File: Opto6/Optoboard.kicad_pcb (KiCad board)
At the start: 2 copper layers, 91.4 x 33 mm, 54 parts, among them J1 S1 Connector, J2 S2 Connector, J3 S3 Connector, J4 S4 Connector, J6 S5 Connector, J7 S6 Connector, P1 CONN_01X08, Q1 IRLR024NPBF, U1 6N135, U2 6N135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

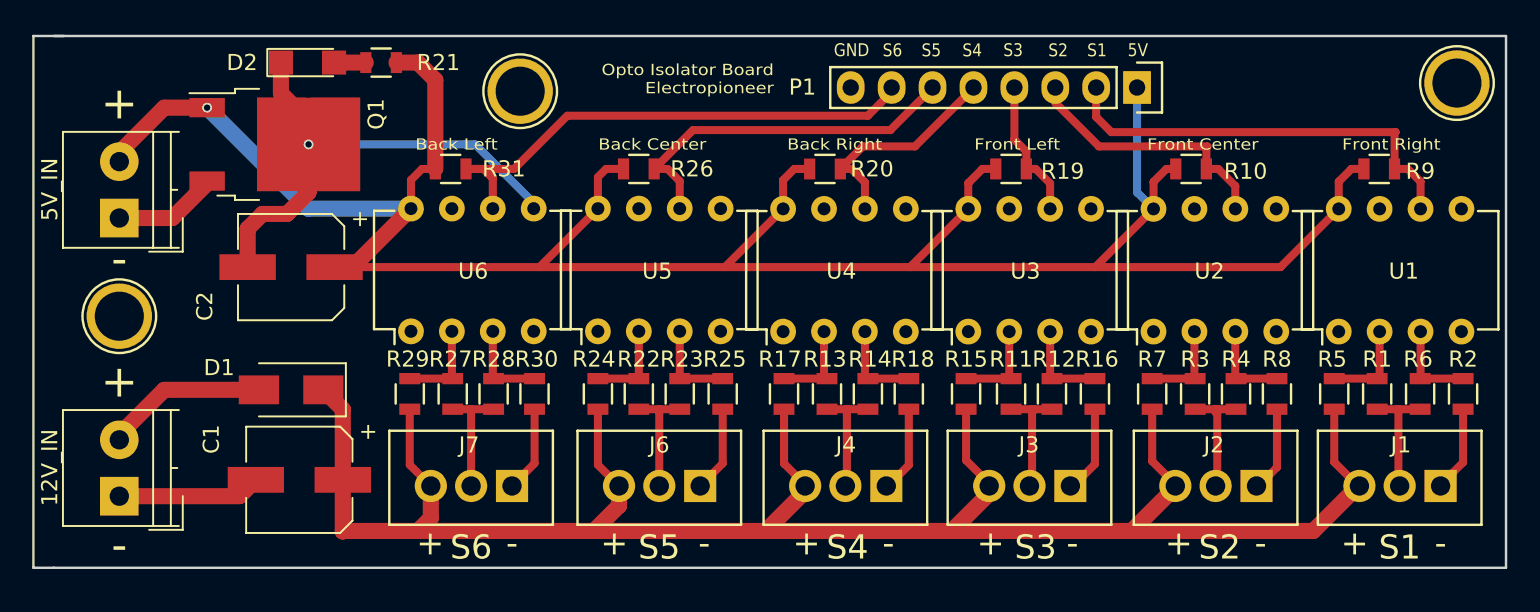
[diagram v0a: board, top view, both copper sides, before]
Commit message: Added opto4 and opto6 updated images
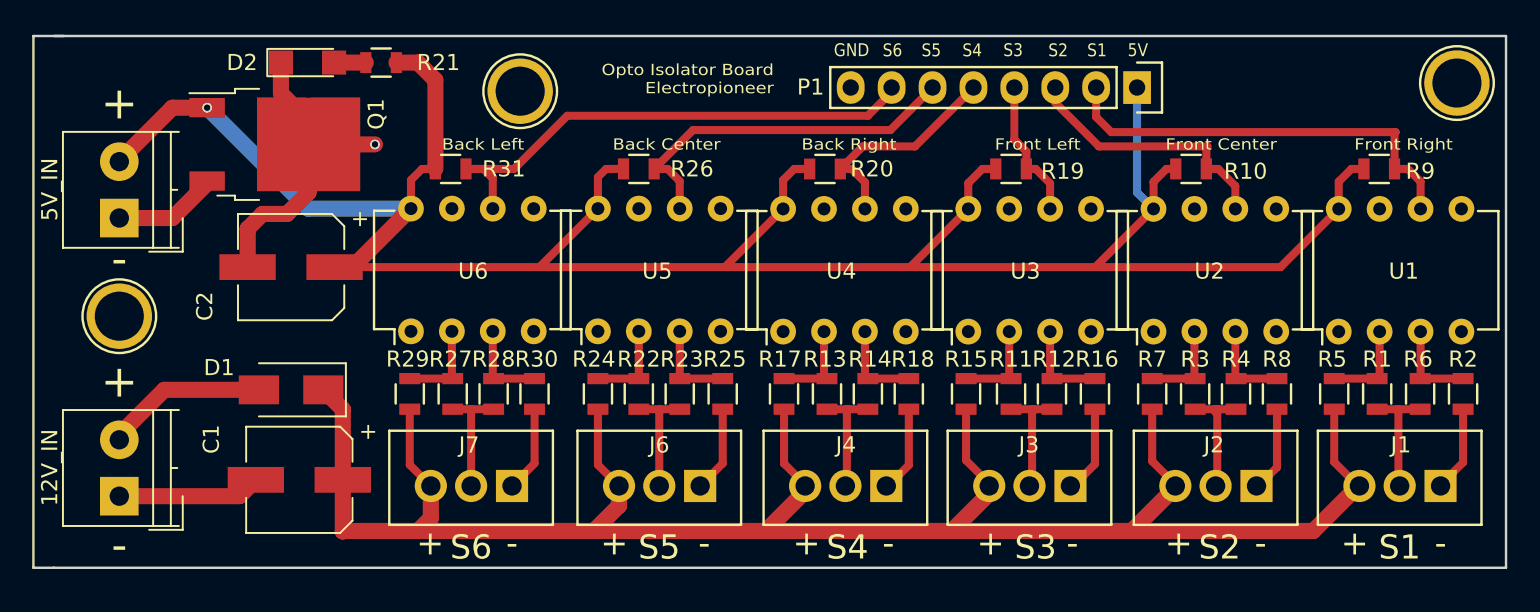
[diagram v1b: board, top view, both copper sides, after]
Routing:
- net GND: track 72.6 -> 61.2 mm
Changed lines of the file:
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@@
     (links 107)
     (no_connects 0)
-    (area 136.373799 90.069599 227.963801 123.239601)
+    (area 136.3398 88.236666 228.2968 125.673172)
     (thickness 1.6)
-    (drawings 46)
-    (tracks 221)
+    (drawings 49)
+    (tracks 220)
     (zones 0)
     (modules 54)
@@
     (32 B.Adhes user)
     (33 F.Adhes user)
-    (34 B.Paste user hide)
+    (34 B.Paste user)
     (35 F.Paste user)
     (36 B.SilkS user)
@@
     (38 B.Mask user)
     (39 F.Mask user)
-    (40 Dwgs.User user hide)
+    (40 Dwgs.User user)
     (41 Cmts.User user)
     (42 Eco1.User user)
@@
   )
   (setup
-    (last_trace_width 1)
+    (last_trace_width 0.25)
     (user_trace_width 0.25)
     (user_trace_width 0.5)
@@
     (pad_to_mask_clearance 0.2)
     (aux_axis_origin 0 0)
-    (grid_origin 196.1388 103.4796)
+    (grid_origin 106.2228 55.7276)
     (visible_elements FFFFFF7F)
     (pcbplotparams
@@
     (descr "Through hole pin header")
     (tags "pin header")
-    (fp_text reference P1 (at -0.0254 20.7772 360) (layer F.SilkS)
+    (fp_text reference P1 (at -0.0254 20.2692 360) (layer F.SilkS)
       (effects (font (size 1 1) (thickness 0.15)))
     )
@@
     (pad 1 thru_hole circle (at 0 0) (size 4.064 4.064) (drill 3.048) (layers *.Cu *.Mask F.SilkS))
   )
+  (dimension 3.048 (width 0.3) (layer Dwgs.User)
+    (gr_text "3,048 mm" (at 126.6698 107.5436 270) (layer Dwgs.User)
+      (effects (font (size 1.5 1.5) (thickness 0.3)))
+    )
+    (feature1 (pts (xy 141.7828 109.0676) (xy 128.0338 109.0676)))
+    (feature2 (pts (xy 141.7828 106.0196) (xy 128.0338 106.0196)))
+    (crossbar (pts (xy 130.7338 106.0196) (xy 130.7338 109.0676)))
+    (arrow1a (pts (xy 130.7338 109.0676) (xy 130.147379 107.941096)))
+    (arrow1b (pts (xy 130.7338 109.0676) (xy 131.320221 107.941096)))
+    (arrow2a (pts (xy 130.7338 106.0196) (xy 130.147379 107.146104)))
+    (arrow2b (pts (xy 130.7338 106.0196) (xy 131.320221 107.146104)))
+  )
+  (dimension 91.44 (width 0.3) (layer Dwgs.User)
+    (gr_text "91,440 mm" (at 182.1688 85.8736) (layer Dwgs.User)
+      (effects (font (size 1.5 1.5) (thickness 0.3)))
+    )
+    (feature1 (pts (xy 227.8888 90.1446) (xy 227.8888 84.5236)))
+    (feature2 (pts (xy 136.4488 90.1446) (xy 136.4488 84.5236)))
+    (crossbar (pts (xy 136.4488 87.2236) (xy 227.8888 87.2236)))
+    (arrow1a (pts (xy 227.8888 87.2236) (xy 226.762296 87.810021)))
+    (arrow1b (pts (xy 227.8888 87.2236) (xy 226.762296 86.637179)))
+    (arrow2a (pts (xy 136.4488 87.2236) (xy 137.575304 87.810021)))
+    (arrow2b (pts (xy 136.4488 87.2236) (xy 137.575304 86.637179)))
+  )
+  (dimension 33.02 (width 0.3) (layer Dwgs.User)
+    (gr_text "33,020 mm" (at 231.7788 106.6546 270) (layer Dwgs.User)
+      (effects (font (size 1.5 1.5) (thickness 0.3)))
+    )
+    (feature1 (pts (xy 227.8888 123.1646) (xy 233.1288 123.1646)))
+    (feature2 (pts (xy 227.8888 90.1446) (xy 233.1288 90.1446)))
+    (crossbar (pts (xy 230.4288 90.1446) (xy 230.4288 123.1646)))
+    (arrow1a (pts (xy 230.4288 123.1646) (xy 229.842379 122.038096)))
+    (arrow1b (pts (xy 230.4288 123.1646) (xy 231.015221 122.038096)))
+    (arrow2a (pts (xy 230.4288 90.1446) (xy 229.842379 91.271104)))
+    (arrow2b (pts (xy 230.4288 90.1446) (xy 231.015221 91.271104)))
+  )
   (gr_line (start 136.4488 90.1446) (end 138.3538 90.1446) (angle 90) (layer Edge.Cuts) (width 0.15))
   (gr_line (start 136.4488 123.1646) (end 136.4488 90.1446) (angle 90) (layer Edge.Cuts) (width 0.15))
@@
   (gr_line (start 227.8888 90.1446) (end 227.8888 123.1646) (angle 90) (layer Edge.Cuts) (width 0.15))
   (gr_line (start 137.7188 90.1446) (end 227.8888 90.1446) (angle 90) (layer Edge.Cuts) (width 0.15))
-  (gr_text "Front Right" (at 223.8248 96.8756) (layer F.SilkS)
+  (gr_text "Front Right" (at 224.5868 96.8756) (layer F.SilkS)
     (effects (font (size 0.7 0.8) (thickness 0.175)) (justify right))
   )
-  (gr_text "Front Center" (at 212.5218 96.8756) (layer F.SilkS)
+  (gr_text "Front Center" (at 213.6648 96.8756) (layer F.SilkS)
     (effects (font (size 0.7 0.8) (thickness 0.175)) (justify right))
   )
-  (gr_text "Front Left" (at 200.2028 96.8756) (layer F.SilkS)
+  (gr_text "Front Left" (at 201.4728 96.8756) (layer F.SilkS)
     (effects (font (size 0.7 0.8) (thickness 0.175)) (justify right))
   )
-  (gr_text "Back Right" (at 189.1538 96.8756) (layer F.SilkS)
+  (gr_text "Back Right" (at 190.0428 96.8756) (layer F.SilkS)
     (effects (font (size 0.7 0.8) (thickness 0.175)) (justify right))
   )
-  (gr_text "Back Center" (at 178.2318 96.8756) (layer F.SilkS)
+  (gr_text "Back Center" (at 179.1208 96.8756) (layer F.SilkS)
     (effects (font (size 0.7 0.8) (thickness 0.175)) (justify right))
   )
-  (gr_text "Back Left" (at 165.2778 96.8756) (layer F.SilkS)
+  (gr_text "Back Left" (at 166.9288 96.8756) (layer F.SilkS)
     (effects (font (size 0.7 0.8) (thickness 0.175)) (justify right))
   )
@@
     (effects (font (size 2 2) (thickness 0.3)))
   )
-  (via (at 153.5348 96.8756) (size 0.6) (drill 0.4) (layers F.Cu B.Cu) (net 1))
-  (segment (start 167.513 100.5078) (end 163.8808 96.8756) (width 0.5) (layer B.Cu) (net 1))
-  (segment (start 163.2458 96.8756) (end 163.8808 96.8756) (width 0.5) (layer B.Cu) (net 1))
-  (segment (start 163.2458 96.8756) (end 153.5348 96.8756) (width 0.5) (layer B.Cu) (net 1))
+  (segment (start 153.5348 96.8756) (end 157.6578 96.8756) (width 1) (layer F.Cu) (net 1))
+  (via (at 157.6578 96.8756) (size 0.6) (drill 0.4) (layers F.Cu B.Cu) (net 1))
   (segment (start 167.513 100.5078) (end 167.513 100.8634) (width 0.5) (layer B.Cu) (net 1))
   (segment (start 141.7828 118.7196) (end 149.2428 118.7196) (width 1) (layer F.Cu) (net 1))
@@
   (segment (start 141.7828 114.9096) (end 144.5768 112.1156) (width 1) (layer F.Cu) (net 2))
   (segment (start 144.5768 112.1156) (end 150.4508 112.1156) (width 1) (layer F.Cu) (net 2))
-  (segment (start 207.3548 118.0846) (end 207.3548 118.1716) (width 1) (layer F.Cu) (net 3) (status C00000))
-  (segment (start 207.3548 118.1716) (end 204.6478 120.8786) (width 1) (layer F.Cu) (net 3) (status 400000))
-  (segment (start 195.7978 118.0846) (end 195.7978 118.5526) (width 1) (layer F.Cu) (net 3) (status C00000))
-  (segment (start 195.7978 118.5526) (end 193.4718 120.8786) (width 1) (layer F.Cu) (net 3) (status 400000))
-  (segment (start 184.3678 118.0846) (end 184.3678 118.4256) (width 1) (layer F.Cu) (net 3) (status C00000))
-  (segment (start 184.3678 118.4256) (end 181.9148 120.8786) (width 1) (layer F.Cu) (net 3) (status 400000))
-  (segment (start 172.8108 118.0846) (end 172.8108 119.3146) (width 1) (layer F.Cu) (net 3) (status 400000))
+  (segment (start 207.3548 118.0846) (end 207.3548 118.1716) (width 1) (layer F.Cu) (net 3))
+  (segment (start 207.3548 118.1716) (end 204.6478 120.8786) (width 1) (layer F.Cu) (net 3))
+  (segment (start 195.7978 118.0846) (end 195.7978 118.5526) (width 1) (layer F.Cu) (net 3))
+  (segment (start 195.7978 118.5526) (end 193.4718 120.8786) (width 1) (layer F.Cu) (net 3))
+  (segment (start 184.3678 118.0846) (end 184.3678 118.4256) (width 1) (layer F.Cu) (net 3))
+  (segment (start 184.3678 118.4256) (end 181.9148 120.8786) (width 1) (layer F.Cu) (net 3))
+  (segment (start 172.8108 118.0846) (end 172.8108 119.3146) (width 1) (layer F.Cu) (net 3))
   (segment (start 172.8108 119.3146) (end 171.2468 120.8786) (width 1) (layer F.Cu) (net 3))
-  (segment (start 161.1268 118.0846) (end 161.1268 120.0766) (width 1) (layer F.Cu) (net 3) (status 400000))
+  (segment (start 161.1268 118.0846) (end 161.1268 120.0766) (width 1) (layer F.Cu) (net 3))
   (segment (start 161.1268 120.0766) (end 160.3248 120.8786) (width 1) (layer F.Cu) (net 3))
   (segment (start 155.6588 117.7036) (end 155.6588 113.3236) (width 1) (layer F.Cu) (net 3))
@@
   (segment (start 159.8168 116.7746) (end 161.1268 118.0846) (width 0.5) (layer F.Cu) (net 3))
   (segment (start 184.22 117.895) (end 184.42 118.095) (width 0.5) (layer F.Cu) (net 3))
+  (via (at 147.2348 94.5956) (size 0.6) (drill 0.4) (layers F.Cu B.Cu) (net 4))
+  (segment (start 145.0788 94.5956) (end 147.2348 94.5956) (width 1) (layer F.Cu) (net 4))
+  (segment (start 141.7828 97.8916) (end 145.0788 94.5956) (width 1) (layer F.Cu) (net 4))
+  (segment (start 153.5026 100.8634) (end 159.893 100.8634) (width 1) (layer B.Cu) (net 4))
+  (segment (start 147.2348 94.5956) (end 153.5026 100.8634) (width 1) (layer B.Cu) (net 4))
+  (segment (start 141.7828 97.9476) (end 141.7828 97.8916) (width 1) (layer F.Cu) (net 4))
   (segment (start 204.978 93.345) (end 204.978 99.858) (width 0.5) (layer B.Cu) (net 4))
   (segment (start 204.978 99.858) (end 206 100.88) (width 0.5) (layer B.Cu) (net 4))
@@
   (segment (start 172.0088 98.3996) (end 173.0908 98.3996) (width 0.5) (layer F.Cu) (net 4))
   (segment (start 159.893 100.8634) (end 159.893 99.0854) (width 0.5) (layer F.Cu) (net 4))
+  (segment (start 159.893 99.0854) (end 160.5788 98.3996) (width 0.5) (layer F.Cu) (net 4))
   (segment (start 160.5788 98.3996) (end 161.4068 98.3996) (width 0.5) (layer F.Cu) (net 4))
-  (segment (start 159.893 99.0854) (end 160.5788 98.3996) (width 0.5) (layer F.Cu) (net 4))
-  (via (at 147.2348 94.5956) (size 0.6) (drill 0.4) (layers F.Cu B.Cu) (net 4))
-  (segment (start 144.5708 94.5956) (end 147.2348 94.5956) (width 1) (layer F.Cu) (net 4))
-  (segment (start 141.7828 97.3836) (end 144.5708 94.5956) (width 1) (layer F.Cu) (net 4))
-  (segment (start 153.5026 100.8634) (end 159.893 100.8634) (width 1) (layer B.Cu) (net 4))
-  (segment (start 147.2348 94.5956) (end 153.5026 100.8634) (width 1) (layer B.Cu) (net 4))
   (segment (start 155.1508 104.4956) (end 156.2608 104.4956) (width 1) (layer F.Cu) (net 4))
   (segment (start 156.2608 104.4956) (end 159.893 100.8634) (width 1) (layer F.Cu) (net 4))

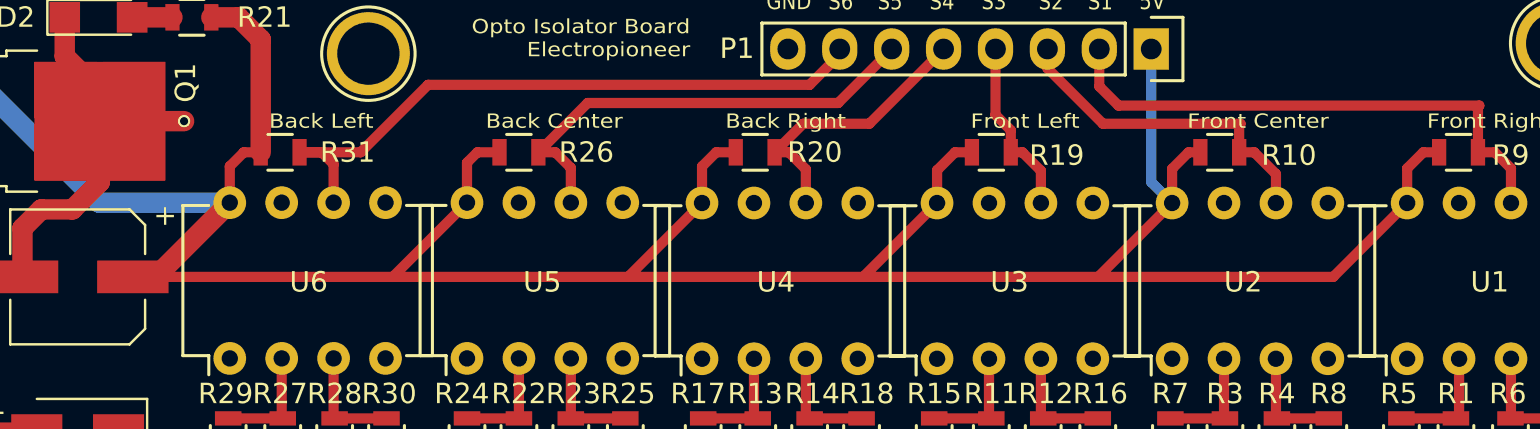
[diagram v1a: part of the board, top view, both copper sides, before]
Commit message: Changed some traces
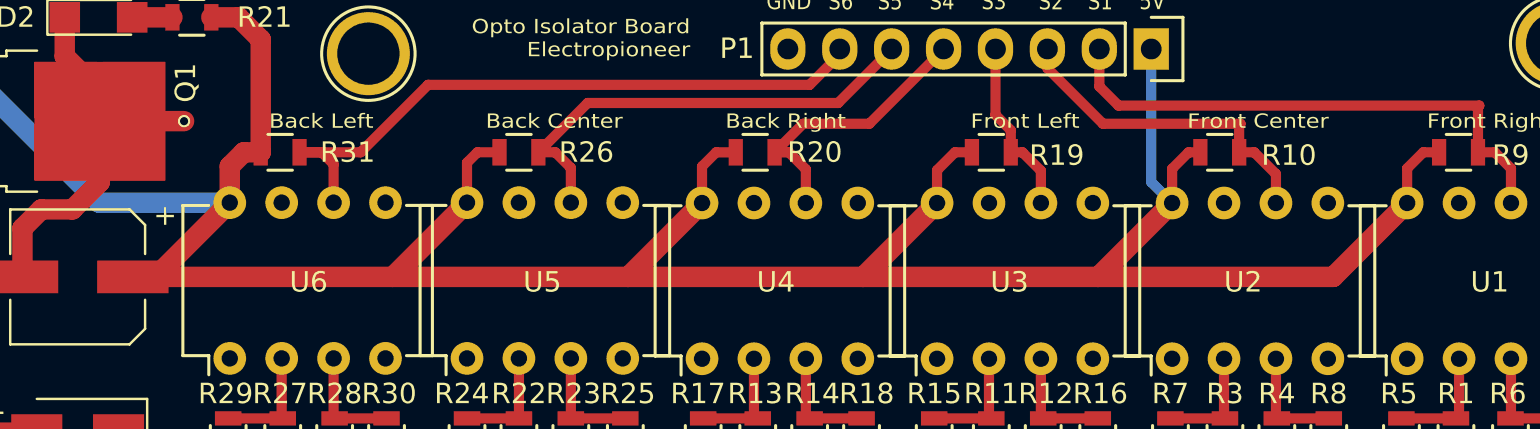
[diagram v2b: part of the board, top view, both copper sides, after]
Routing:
- net +5V: track 151.3 -> 190.2 mm
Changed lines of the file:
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@@
     (links 107)
     (no_connects 0)
-    (area 136.3398 88.236666 228.2968 125.673172)
+    (area 120.734087 84.3736 238.4288 125.673172)
     (thickness 1.6)
     (drawings 49)
-    (tracks 220)
+    (tracks 229)
     (zones 0)
     (modules 54)
@@
   )
   (setup
-    (last_trace_width 0.25)
+    (last_trace_width 1)
     (user_trace_width 0.25)
     (user_trace_width 0.5)
@@
   (segment (start 159.8168 116.7746) (end 161.1268 118.0846) (width 0.5) (layer F.Cu) (net 3))
   (segment (start 184.22 117.895) (end 184.42 118.095) (width 0.5) (layer F.Cu) (net 3))
+  (segment (start 159.893 100.8634) (end 159.893 99.0854) (width 1) (layer F.Cu) (net 4) (status 400000))
+  (segment (start 159.893 99.0854) (end 160.5788 98.3996) (width 1) (layer F.Cu) (net 4))
+  (segment (start 160.5788 98.3996) (end 161.4068 98.3996) (width 1) (layer F.Cu) (net 4) (status 800000))
+  (segment (start 202.3844 104.4956) (end 213.8844 104.4956) (width 1) (layer F.Cu) (net 4))
+  (segment (start 213.8844 104.4956) (end 217.5 100.88) (width 1) (layer F.Cu) (net 4) (status 800000))
+  (segment (start 190.8844 104.4956) (end 202.3844 104.4956) (width 1) (layer F.Cu) (net 4))
+  (segment (start 202.3844 104.4956) (end 206 100.88) (width 1) (layer F.Cu) (net 4) (status 800000))
+  (segment (start 179.3748 104.4956) (end 190.8844 104.4956) (width 1) (layer F.Cu) (net 4))
+  (segment (start 190.8844 104.4956) (end 194.5 100.88) (width 1) (layer F.Cu) (net 4) (status 800000))
+  (segment (start 167.8686 104.4956) (end 179.3748 104.4956) (width 1) (layer F.Cu) (net 4))
+  (segment (start 179.3748 104.4956) (end 179.3844 104.4956) (width 1) (layer F.Cu) (net 4))
+  (segment (start 179.3844 104.4956) (end 183 100.88) (width 1) (layer F.Cu) (net 4) (status 800000))
+  (segment (start 155.1508 104.4956) (end 167.8686 104.4956) (width 1) (layer F.Cu) (net 4) (status 400000))
+  (segment (start 167.8686 104.4956) (end 171.5008 100.8634) (width 1) (layer F.Cu) (net 4) (status 800000))
   (via (at 147.2348 94.5956) (size 0.6) (drill 0.4) (layers F.Cu B.Cu) (net 4))
   (segment (start 145.0788 94.5956) (end 147.2348 94.5956) (width 1) (layer F.Cu) (net 4))
@@
   (segment (start 204.978 93.345) (end 204.978 99.858) (width 0.5) (layer B.Cu) (net 4))
   (segment (start 204.978 99.858) (end 206 100.88) (width 0.5) (layer B.Cu) (net 4))
-  (segment (start 202.3844 104.4956) (end 213.8844 104.4956) (width 0.5) (layer F.Cu) (net 4))
   (segment (start 213.8844 104.4956) (end 217.5 100.88) (width 0.5) (layer F.Cu) (net 4))
-  (segment (start 190.8844 104.4956) (end 202.3844 104.4956) (width 0.5) (layer F.Cu) (net 4))
   (segment (start 202.3844 104.4956) (end 206 100.88) (width 0.5) (layer F.Cu) (net 4))
   (segment (start 179.3844 104.4956) (end 190.8844 104.4956) (width 0.5) (layer F.Cu) (net 4))
   (segment (start 190.8844 104.4956) (end 194.5 100.88) (width 0.5) (layer F.Cu) (net 4))
-  (segment (start 167.8686 104.4956) (end 179.3844 104.4956) (width 0.5) (layer F.Cu) (net 4))
   (segment (start 179.3844 104.4956) (end 183 100.88) (width 0.5) (layer F.Cu) (net 4))
-  (segment (start 155.1508 104.4956) (end 167.8686 104.4956) (width 0.5) (layer F.Cu) (net 4))
   (segment (start 167.8686 104.4956) (end 171.5008 100.8634) (width 0.5) (layer F.Cu) (net 4))
   (segment (start 217.5 100.88) (end 217.5 99.1868) (width 0.5) (layer F.Cu) (net 4))
@@
   (segment (start 171.5008 98.9076) (end 172.0088 98.3996) (width 0.5) (layer F.Cu) (net 4))
   (segment (start 172.0088 98.3996) (end 173.0908 98.3996) (width 0.5) (layer F.Cu) (net 4))
-  (segment (start 159.893 100.8634) (end 159.893 99.0854) (width 0.5) (layer F.Cu) (net 4))
   (segment (start 159.893 99.0854) (end 160.5788 98.3996) (width 0.5) (layer F.Cu) (net 4))
   (segment (start 160.5788 98.3996) (end 161.4068 98.3996) (width 0.5) (layer F.Cu) (net 4))
